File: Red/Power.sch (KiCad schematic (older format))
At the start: 7 parts, among them J801 Conn_01x02, U802 AZ1117-3.3, U803 AZ1117-5.0

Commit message: Post design review
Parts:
- renumbered C802 to C201, C803 to C202, C805 to C203, C806 to C204, J801 to J201, U802 to U201, U803 to U202
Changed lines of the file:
@@
 $EndDescr
 $Comp
-L Connector_Generic:Conn_01x02 J801
+L Connector_Generic:Conn_01x02 J201
 U 1 1 5ECBBA43
 P 3500 3350
-F 0 "J801" H 3418 3025 50  0000 C CNN
+F 0 "J201" H 3418 3025 50  0000 C CNN
 F 1 "Conn_01x02" H 3418 3116 50  0000 C CNN
 F 2 "Connector_AMASS:AMASS_XT30PW-M_1x02_P2.50mm_Horizontal" H 3500 3350 50  0001 C CNN
@@
 $EndComp
 $Comp
-L power:GND #PWR0802
+L power:GND #PWR0202
 U 1 1 5ECBC98C
 P 3850 3500
-F 0 "#PWR0802" H 3850 3250 50  0001 C CNN
+F 0 "#PWR0202" H 3850 3250 50  0001 C CNN
 F 1 "GND" H 3855 3327 50  0000 C CNN
 F 2 "" H 3850 3500 50  0001 C CNN
@@
 $EndComp
 $Comp
-L power:+BATT #PWR0801
+L power:+BATT #PWR0201
 U 1 1 5ECBD48F
 P 3850 3100
-F 0 "#PWR0801" H 3850 2950 50  0001 C CNN
+F 0 "#PWR0201" H 3850 2950 50  0001 C CNN
 F 1 "+BATT" H 3865 3273 50  0000 C CNN
 F 2 "" H 3850 3100 50  0001 C CNN
@@
 	3850 3350 3850 3500
 $Comp
-L power:PWR_FLAG #FLG0801
+L power:PWR_FLAG #FLG0201
 U 1 1 5ECC01CB
 P 3850 3250
-F 0 "#FLG0801" H 3850 3325 50  0001 C CNN
+F 0 "#FLG0201" H 3850 3325 50  0001 C CNN
 F 1 "PWR_FLAG" V 3850 3378 50  0000 L CNN
 F 2 "" H 3850 3250 50  0001 C CNN
@@
 $EndComp
 $Comp
-L power:PWR_FLAG #FLG0802
+L power:PWR_FLAG #FLG0202
 U 1 1 5ECC0E37
 P 3850 3350
-F 0 "#FLG0802" H 3850 3425 50  0001 C CNN
+F 0 "#FLG0202" H 3850 3425 50  0001 C CNN
 F 1 "PWR_FLAG" V 3850 3478 50  0000 L CNN
 F 2 "" H 3850 3350 50  0001 C CNN
@@
 Connection ~ 3850 3350
 $Comp
-L Regulator_Linear:AZ1117-3.3 U802
+L Regulator_Linear:AZ1117-3.3 U201
 U 1 1 5ECC7B03
 P 5050 3300
-F 0 "U802" H 5050 3542 50  0000 C CNN
+F 0 "U201" H 5050 3542 50  0000 C CNN
 F 1 "AZ1117-3.3" H 5050 3451 50  0000 C CNN
 F 2 "Package_TO_SOT_SMD:SOT-223" H 5050 3550 50  0001 C CIN
@@
 $EndComp
 $Comp
-L Regulator_Linear:AZ1117-5.0 U803
+L Regulator_Linear:AZ1117-5.0 U202
 U 1 1 5ECC8529
 P 5050 4150
-F 0 "U803" H 5050 4392 50  0000 C CNN
+F 0 "U202" H 5050 4392 50  0000 C CNN
 F 1 "AZ1117-5.0" H 5050 4301 50  0000 C CNN
 F 2 "Package_TO_SOT_SMD:SOT-223" H 5050 4400 50  0001 C CIN
@@
 $EndComp
 $Comp
-L Device:C C802
+L Device:C C201
 U 1 1 5ECD4A20
 P 4500 3450
-F 0 "C802" H 4615 3496 50  0000 L CNN
+F 0 "C201" H 4615 3496 50  0000 L CNN
 F 1 "10uF" H 4615 3405 50  0000 L CNN
 F 2 "Capacitor_SMD:C_0805_2012Metric_Pad1.15x1.40mm_HandSolder" H 4538 3300 50  0001 C CNN
@@
 $EndComp
 $Comp
-L Device:C C803
+L Device:C C202
 U 1 1 5ECD53F3
 P 4500 4300
-F 0 "C803" H 4615 4346 50  0000 L CNN
+F 0 "C202" H 4615 4346 50  0000 L CNN
 F 1 "10uF" H 4615 4255 50  0000 L CNN
 F 2 "Capacitor_SMD:C_0805_2012Metric_Pad1.15x1.40mm_HandSolder" H 4538 4150 50  0001 C CNN
@@
 $EndComp
 $Comp
-L Device:C C805
+L Device:C C203
 U 1 1 5ECD65E2
 P 5600 3450
-F 0 "C805" H 5715 3496 50  0000 L CNN
+F 0 "C203" H 5715 3496 50  0000 L CNN
 F 1 "22uF" H 5715 3405 50  0000 L CNN
 F 2 "Capacitor_SMD:C_0603_1608Metric_Pad1.05x0.95mm_HandSolder" H 5638 3300 50  0001 C CNN
@@
 $EndComp
 $Comp
-L Device:C C806
+L Device:C C204
 U 1 1 5ECD6CF1
 P 5600 4300
-F 0 "C806" H 5715 4346 50  0000 L CNN
+F 0 "C204" H 5715 4346 50  0000 L CNN
 F 1 "22uF" H 5715 4255 50  0000 L CNN
 F 2 "Capacitor_SMD:C_0603_1608Metric_Pad1.05x0.95mm_HandSolder" H 5638 4150 50  0001 C CNN
@@
 	5050 4450 5600 4450
 $Comp
-L power:+BATT #PWR0804
+L power:+BATT #PWR0203
 U 1 1 5ECD8F1D
 P 4500 3200
-F 0 "#PWR0804" H 4500 3050 50  0001 C CNN
+F 0 "#PWR0203" H 4500 3050 50  0001 C CNN
 F 1 "+BATT" H 4515 3373 50  0000 C CNN
 F 2 "" H 4500 3200 50  0001 C CNN
@@
 $EndComp
 $Comp
-L power:+BATT #PWR0805
+L power:+BATT #PWR0204
 U 1 1 5ECD948E
 P 4500 4050
-F 0 "#PWR0805" H 4500 3900 50  0001 C CNN
+F 0 "#PWR0204" H 4500 3900 50  0001 C CNN
 F 1 "+BATT" H 4515 4223 50  0000 C CNN
 F 2 "" H 4500 4050 50  0001 C CNN
@@
 	5600 4150 5350 4150
 $Comp
-L power:+5V #PWR0808
+L power:+5V #PWR0208
 U 1 1 5ECDA5EE
 P 5600 4150
-F 0 "#PWR0808" H 5600 4000 50  0001 C CNN
+F 0 "#PWR0208" H 5600 4000 50  0001 C CNN
 F 1 "+5V" H 5615 4323 50  0000 C CNN
 F 2 "" H 5600 4150 50  0001 C CNN
@@
 Connection ~ 5600 4150
 $Comp
-L power:+3.3V #PWR0807
+L power:+3.3V #PWR0207
 U 1 1 5ECDD508
 P 5600 3300
-F 0 "#PWR0807" H 5600 3150 50  0001 C CNN
+F 0 "#PWR0207" H 5600 3150 50  0001 C CNN
 F 1 "+3.3V" H 5615 3473 50  0000 C CNN
 F 2 "" H 5600 3300 50  0001 C CNN
@@
 Connection ~ 5600 3300
 $Comp
-L power:GND #PWR0102
+L power:GND #PWR0205
 U 1 1 5ECF7238
 P 5050 3600
-F 0 "#PWR0102" H 5050 3350 50  0001 C CNN
+F 0 "#PWR0205" H 5050 3350 50  0001 C CNN
 F 1 "GND" H 5055 3427 50  0000 C CNN
 F 2 "" H 5050 3600 50  0001 C CNN
@@
 $EndComp
 $Comp
-L power:GND #PWR0103
+L power:GND #PWR0206
 U 1 1 5ECF79AC
 P 5050 4450
-F 0 "#PWR0103" H 5050 4200 50  0001 C CNN
+F 0 "#PWR0206" H 5050 4200 50  0001 C CNN
 F 1 "GND" H 5055 4277 50  0000 C CNN
 F 2 "" H 5050 4450 50  0001 C CNN

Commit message: Swapped USBC connector out for one that was available, minor Silkscreen tweaks
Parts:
- U201: digikey AZ1117CH-3.3TRG1DITR-ND -> AZ1117CH-3.3TRG1DICT-ND
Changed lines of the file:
@@
 F 2 "Package_TO_SOT_SMD:SOT-223" H 5050 3550 50  0001 C CIN
 F 3 "https://www.diodes.com/assets/Datasheets/AZ1117.pdf" H 5050 3300 50  0001 C CNN
-F 4 "AZ1117CH-3.3TRG1DITR-ND" H 5050 3300 50  0001 C CNN "digikey"
+F 4 "AZ1117CH-3.3TRG1DICT-ND" H 5050 3300 50  0001 C CNN "digikey"
 	1    5050 3300
 	1    0    0    -1

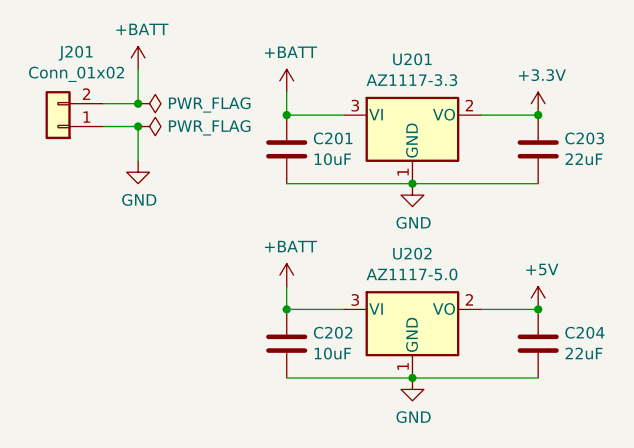
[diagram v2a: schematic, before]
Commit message: Created schematic changes for Red V1.1
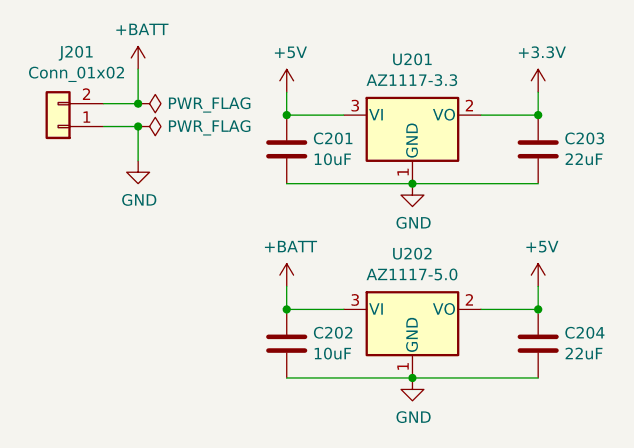
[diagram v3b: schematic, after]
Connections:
- net +5V: now also C201.1, U201.3 (VI)
- net +BATT: no longer C201.1, U201.3 (VI)
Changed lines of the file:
@@
 	5050 4450 5600 4450
-$Comp
-L power:+BATT #PWR0203
-U 1 1 5ECD8F1D
-P 4500 3200
-F 0 "#PWR0203" H 4500 3050 50  0001 C CNN
-F 1 "+BATT" H 4515 3373 50  0000 C CNN
-F 2 "" H 4500 3200 50  0001 C CNN
-F 3 "" H 4500 3200 50  0001 C CNN
-	1    4500 3200
-	1    0    0    -1
-$EndComp
 $Comp
 L power:+BATT #PWR0204
@@
 L power:+5V #PWR0208
 U 1 1 5ECDA5EE
-P 5600 4150
-F 0 "#PWR0208" H 5600 4000 50  0001 C CNN
-F 1 "+5V" H 5615 4323 50  0000 C CNN
-F 2 "" H 5600 4150 50  0001 C CNN
-F 3 "" H 5600 4150 50  0001 C CNN
-	1    5600 4150
+P 5600 4050
+F 0 "#PWR0208" H 5600 3900 50  0001 C CNN
+F 1 "+5V" H 5615 4223 50  0000 C CNN
+F 2 "" H 5600 4050 50  0001 C CNN
+F 3 "" H 5600 4050 50  0001 C CNN
+	1    5600 4050
 	1    0    0    -1
 $EndComp
@@
 L power:+3.3V #PWR0207
 U 1 1 5ECDD508
-P 5600 3300
-F 0 "#PWR0207" H 5600 3150 50  0001 C CNN
-F 1 "+3.3V" H 5615 3473 50  0000 C CNN
-F 2 "" H 5600 3300 50  0001 C CNN
-F 3 "" H 5600 3300 50  0001 C CNN
-	1    5600 3300
+P 5600 3200
+F 0 "#PWR0207" H 5600 3050 50  0001 C CNN
+F 1 "+3.3V" H 5615 3373 50  0000 C CNN
+F 2 "" H 5600 3200 50  0001 C CNN
+F 3 "" H 5600 3200 50  0001 C CNN
+	1    5600 3200
 	1    0    0    -1
 $EndComp
-Connection ~ 5600 3300
 $Comp
 L power:GND #PWR0205
@@
 	1    0    0    -1
 $EndComp
+$Comp
+L power:+5V #PWR?
+U 1 1 5EEF02BB
+P 4500 3200
+F 0 "#PWR?" H 4500 3050 50  0001 C CNN
+F 1 "+5V" H 4515 3373 50  0000 C CNN
+F 2 "" H 4500 3200 50  0001 C CNN
+F 3 "" H 4500 3200 50  0001 C CNN
+	1    4500 3200
+	1    0    0    -1
+$EndComp
+Wire Wire Line
+	5600 4050 5600 4150
+Wire Wire Line
+	5600 3200 5600 3300
+Connection ~ 5600 3300
 $EndSCHEMATC
